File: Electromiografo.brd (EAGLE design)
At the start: 213 x 118.1 mm, 41 parts, among them IC1 ESP32-S3-WROOM-1-N16R8, IC10 LMV321IDBVRG4, IC2 MCP73831T-2DCI_OT, IC3 741G3157DBVR, IC4 LP38692MP-3.3_NOPB, IC5 REF2033AIDDCT, IC6 LMV321IDBVRG4, IC7 LMV321IDBVRG4, IC8 LMV321IDBVRG4, IC9 AD8223ARMZ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

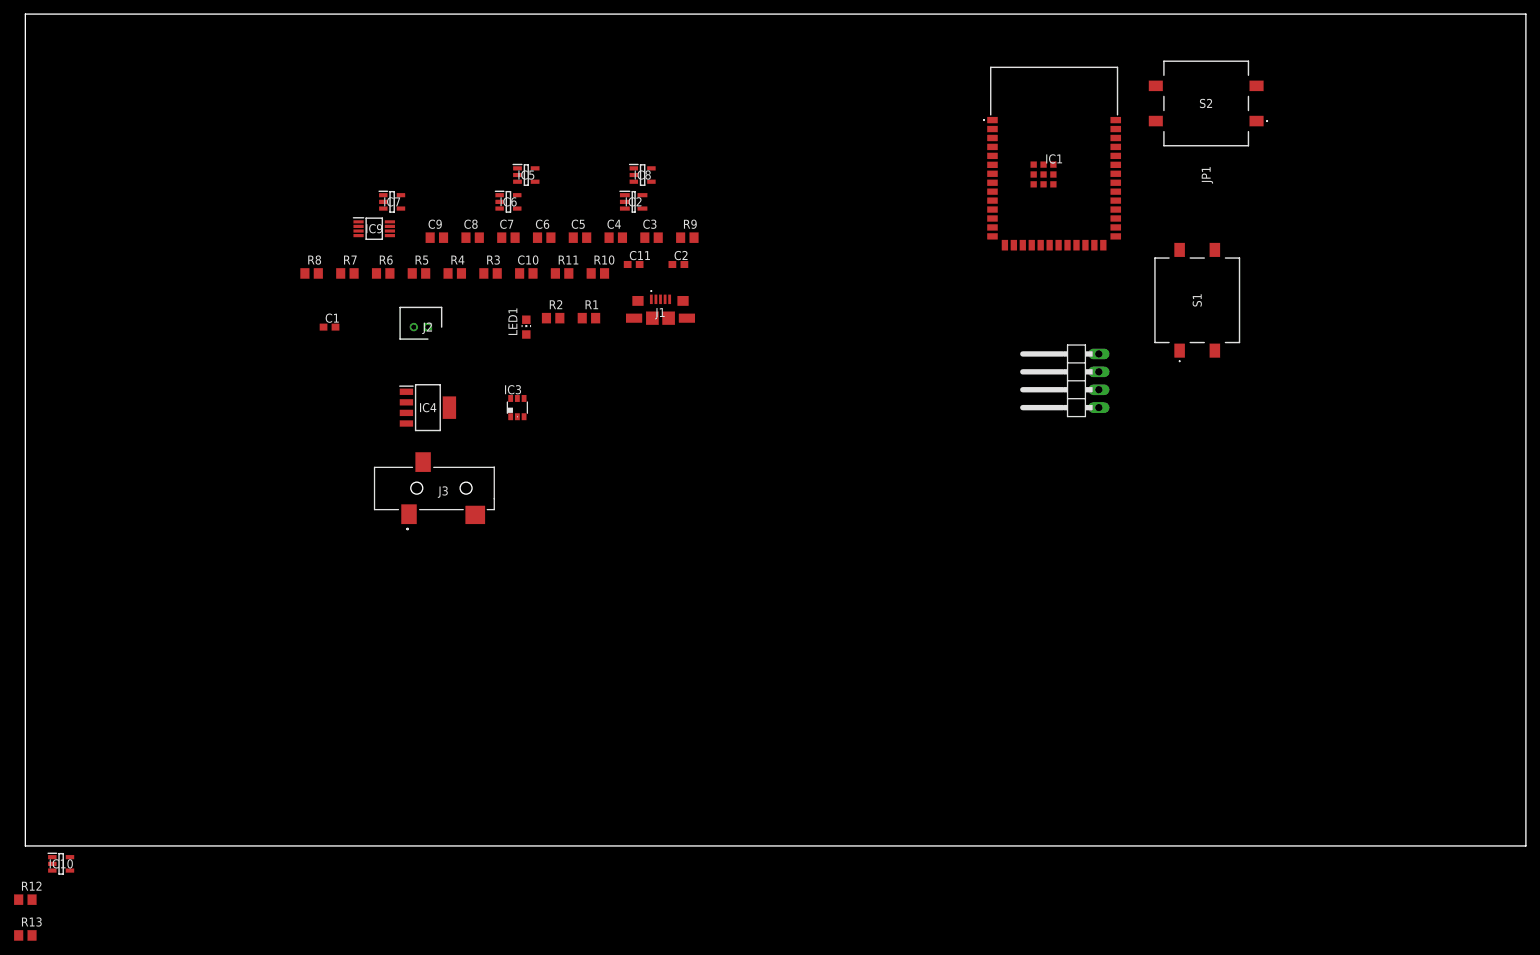
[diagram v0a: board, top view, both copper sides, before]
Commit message: Se ubicaron los elementos en la pcb
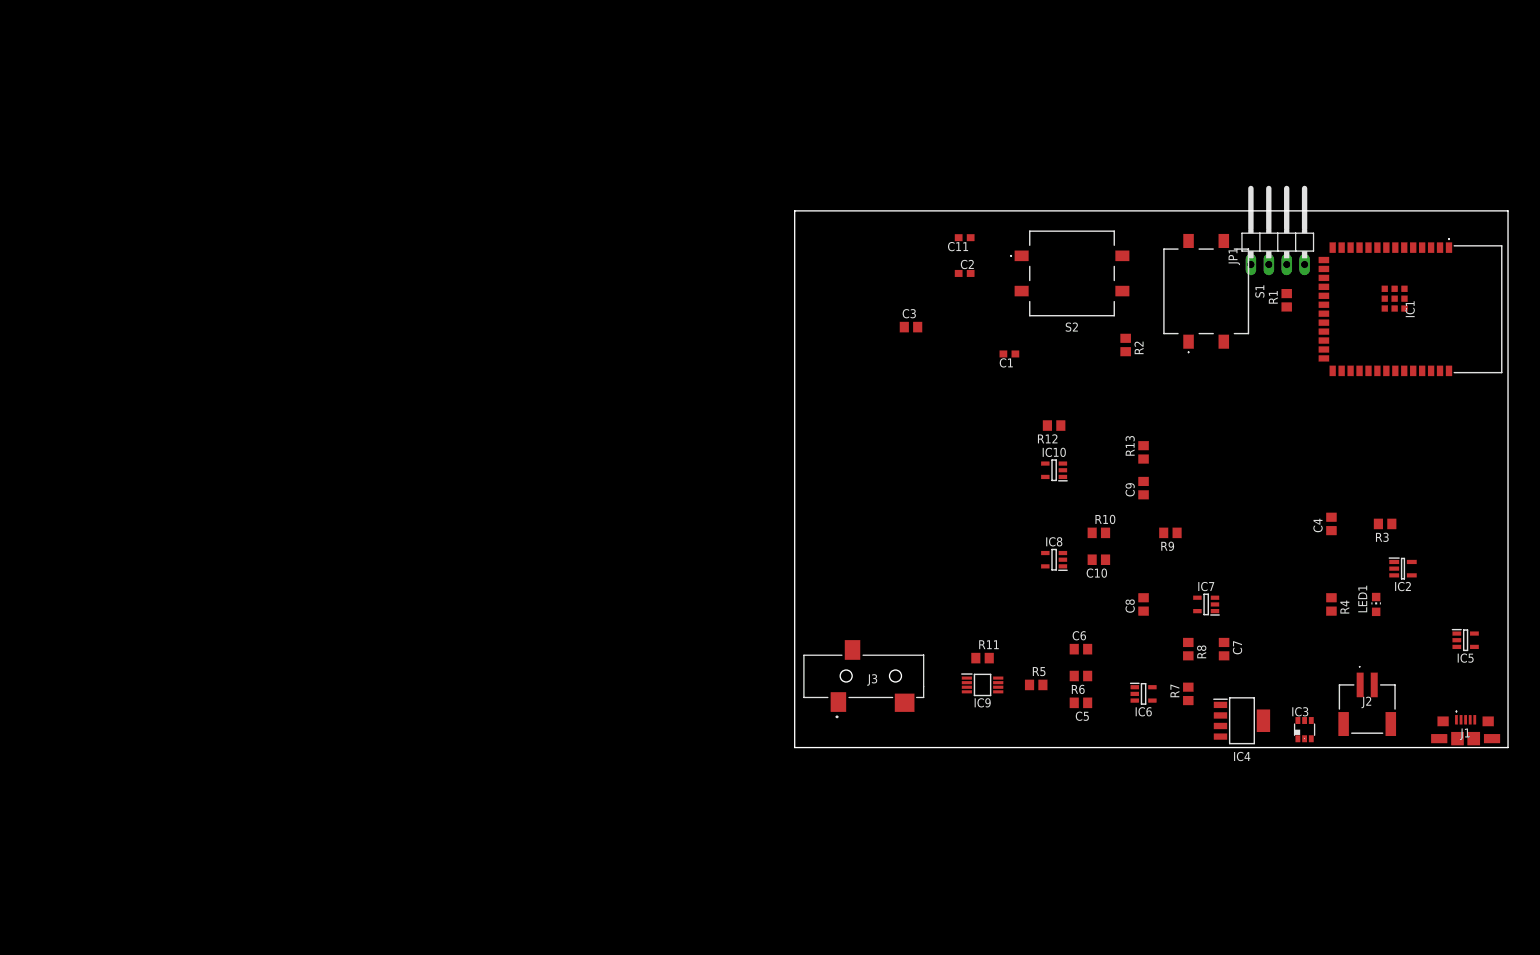
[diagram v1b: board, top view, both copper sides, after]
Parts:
- J2: value B2B-PH-K-S_LF__SN_ -> 1769; device SamacSys_Parts:SHDR2W50P0X200_1X2_590X450X600 -> SamacSys_Parts:1769
- moved R13 172.9 mm to (49.5, 41.9), turned to 90 degrees
- moved R12 160.8 mm to (36.8, 45.7), turned to 180 degrees
- moved IC10 151.6 mm to (36.8, 39.4), turned to 180 degrees
- moved IC5 148.8 mm to (95.2, 15.2)
- moved J2 142.7 mm to (81.3, 8.89)
- moved R8 135.4 mm to (55.9, 14.0), turned to 270 degrees
- moved R7 133.5 mm to (55.9, 7.62), turned to 90 degrees
- moved R4 133.0 mm to (76.2, 20.3), turned to 270 degrees
- moved R3 131.9 mm to (83.8, 31.8), turned to 180 degrees
- moved J1 128.9 mm to (95.2, 1.27)
- moved IC7 128.9 mm to (58.4, 20.3), turned to 180 degrees
- moved LED1 126.9 mm to (82.5, 20.3)
- moved IC4 123.8 mm to (63.5, 3.81)
- moved IC2 121.0 mm to (86.4, 25.4)
- moved IC3 120.8 mm to (72.4, 2.54)
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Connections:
- net +BAT: now also J2.3; no longer J2.1
- net GND: now also J2.4; no longer J2.2
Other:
- board size 213 x 118.1 mm -> 101.3 x 76.2 mm
